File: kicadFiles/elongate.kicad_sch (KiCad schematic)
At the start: 324 parts, among them J1 Wurth 632723300011, Q1 AO3401A, Q2 DTC123JKAT146, Q3 DTC123JKAT146, SW1 MX100, SW10 MX100, SW11 MX100, SW12 MX100, SW13 MX100, SW14 MX100, SW15 MX100, SW16 MX125, SW17 MX100, SW18 MX100, SW19 MX100, SW2 MX100, SW20 MX100, SW21 MX100, SW22 MX100, SW23 MX100, SW24 MX100, SW25 MX100, SW26 MX175, SW27 MX100, SW28 MX100, SW29 MX100, SW3 MX100, SW30 MX175, SW31 MX100, SW32 MX100, SW33 MX100, SW34 MX100, SW35 MX100, SW36 MX100, SW37 MX100, SW38 MX100, SW39 MX125, SW4 MX100, SW40 MX125, SW41 MX100, SW42 MX125, SW43 MX225, SW44 MX275, SW45 MX100, SW46 MX100, SW47 MX100, SW48 MX100, SW49 MX100, SW5 MX100, SW50 MX100, SW51 MX100, SW52 MX100, SW53 MX100, SW54 MX100, SW55 K2-1187SQ-A4SW-06, SW6 MX100, SW7 MX100, SW8 MX100, SW9 MX100, U1 TXS0101, U2 STM32F072CBT6, U3 TPD4E05U06DQAR, U4 MCP1700T-3302E/TT, X1 Conn_01x6, X2 SWD Pins

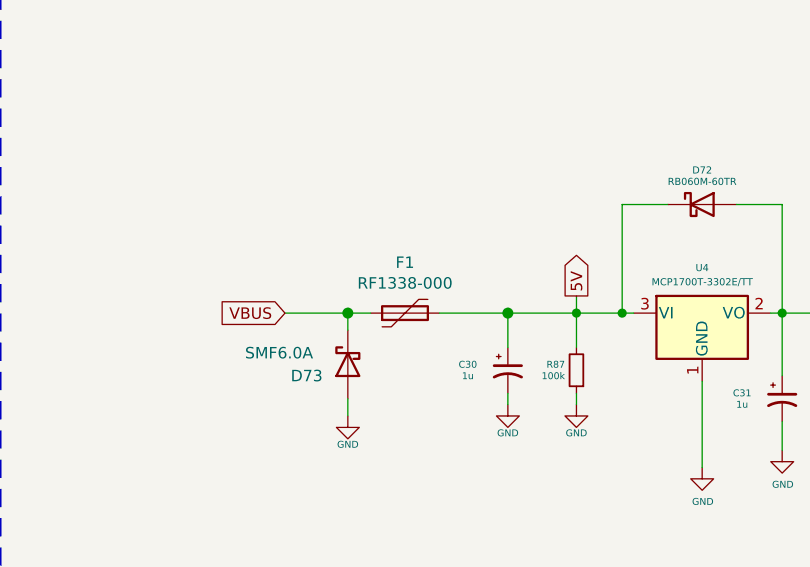
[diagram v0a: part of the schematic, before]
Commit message: Updated component metatada
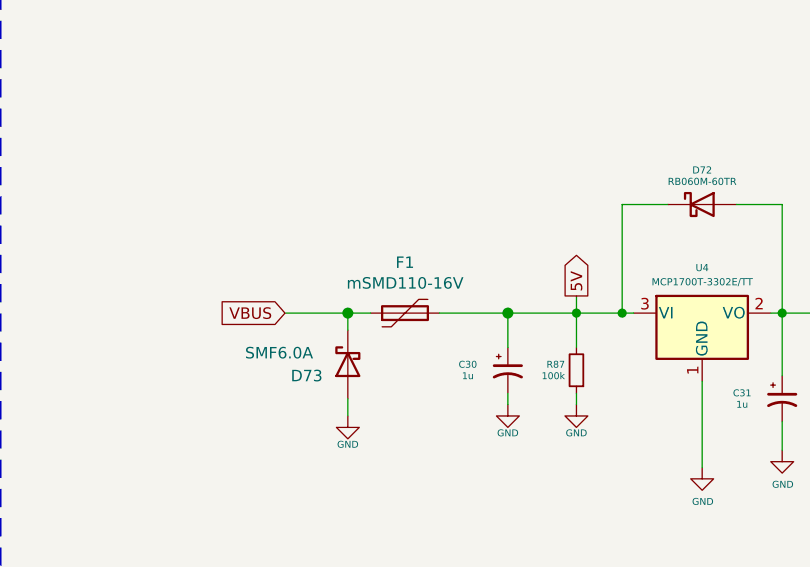
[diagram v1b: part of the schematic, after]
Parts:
- C1, C10, C11, C12, C13, C14, C15, C16, C17, C18, C19, C2, C20, C23, C24, C25, C26, C27, C28, C29, C3, C32, C4, C5, C6, C7, C8, C9: Rating (none) -> MLCC 10V or more
- C21, C22: Rating MLCC 0805 10V or more -> MLCC 10V or more
- C30, C31: Rating (none) -> Tantallum 10V or more
- D1, D10, D11, D12, D13, D14, D15, D16, D2, D3, D4, D5, D6, D7, D8, D9: Rating (none) -> Intelligent integrated controller RGB LED
- D17, D18, D19, D20, D21, D22, D23, D24, D25, D26, D27, D28, D29, D30, D31, D32, D33, D34, D35, D36, D37, D38, D39, D40, D41, D42, D43, D44, D45, D46, D47, D48, D49, D50, D51, D52, D53, D54, D55, D56, D57, D58, D59, D60, D61, D62, D63, D64, D65, D66, D67, D68, D69, D70, D71: Rating (none) -> Small signal switching diode
- D72: Rating (none) -> Power rectifier schottky diode
- D73: Rating (none) -> Unidirectional 6.0V TVS
- F1: value RF1338-000 -> mSMD110-16V; LCSC Part Number C207188 -> C435458; Manufacturer Littelfuse -> Techfuse; Manufacturer Part Number RF1338-000 -> mSMD110-16V; Rating (none) -> 2.2A trip 1.1A hold PTC fuse
- J1: Rating (none) -> WR-COM USB3.1 Type C SuperSpeed USB connector
- Q1: Rating (none) -> P-channel switching MOSFET
- Q2, Q3: Rating (none) -> PNP digital transistor
- SW55: Rating (none) -> 5x5mm tactile switch
- U1: Rating (none) -> 1-bit bidirectional level translator
- U2: Rating (none) -> ARM Cortex M0+ 128kB flash microncontroller
- U3: Rating (none) -> Unidicrectional 6V ultra-fast ESD protection
- U4: Rating (none) -> Fixed 3.3V low dropout regulator
